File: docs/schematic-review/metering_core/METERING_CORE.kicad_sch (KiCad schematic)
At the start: 56 parts, among them U2 ATM90E26-YU, U4 ISO6721BD, U5 MAX3487E

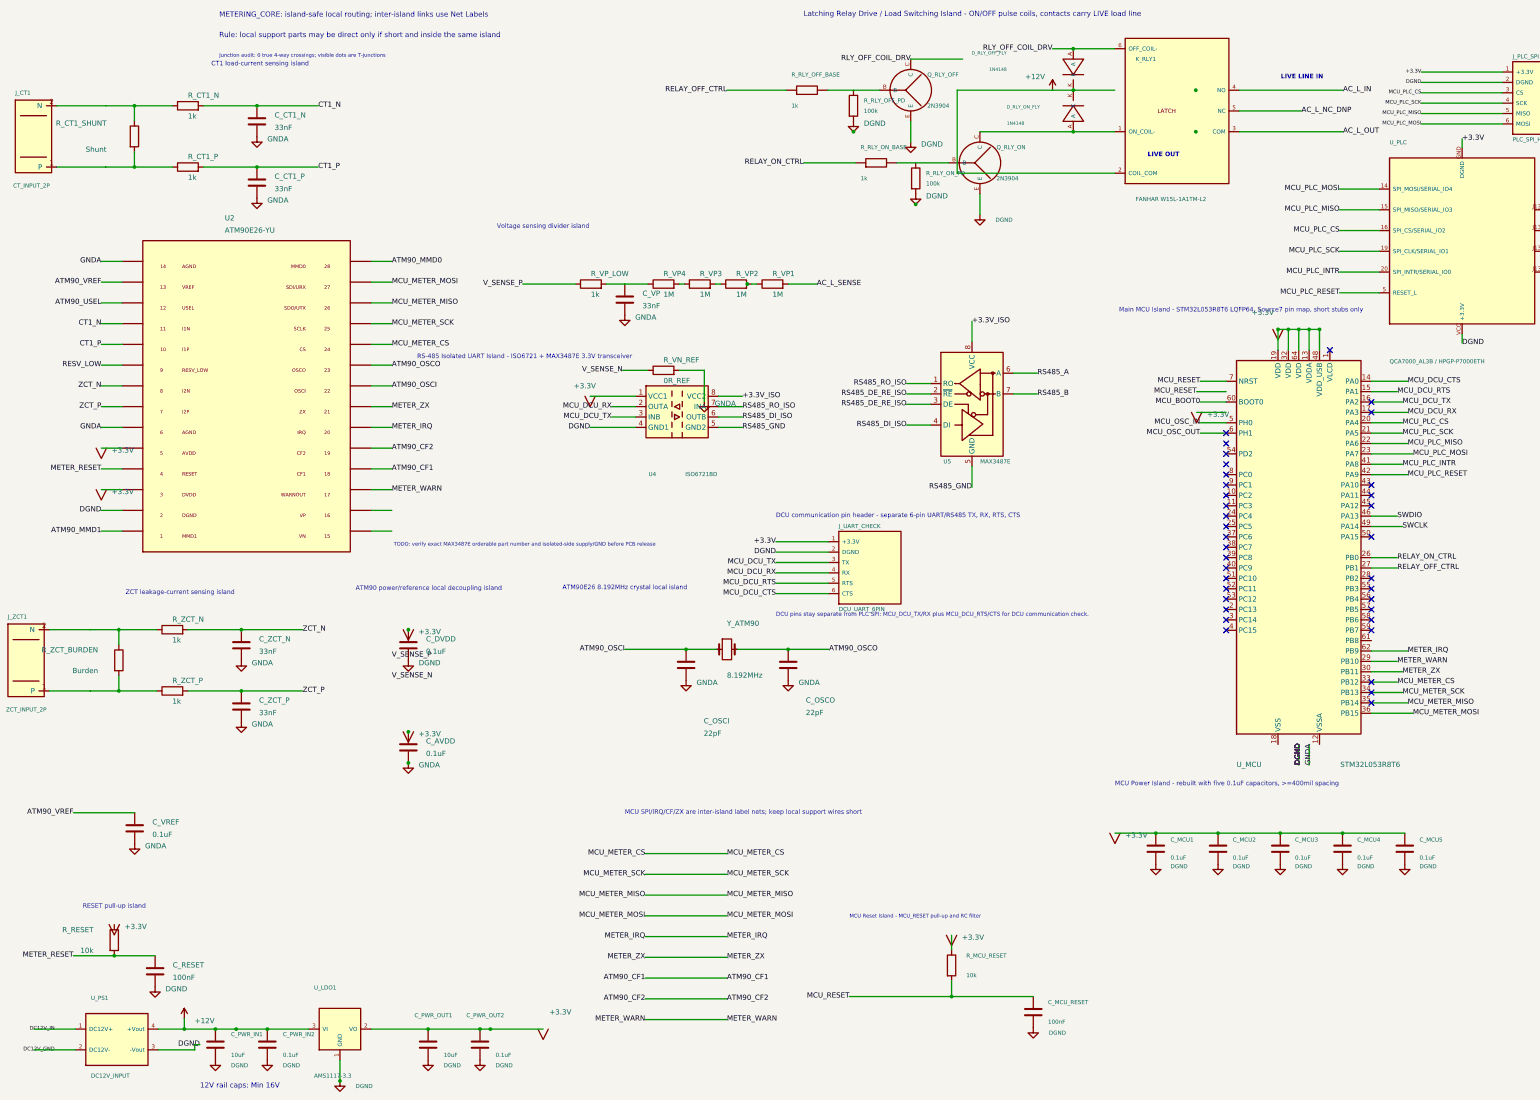
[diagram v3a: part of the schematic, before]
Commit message: Resolve metering schematic ERC review errors
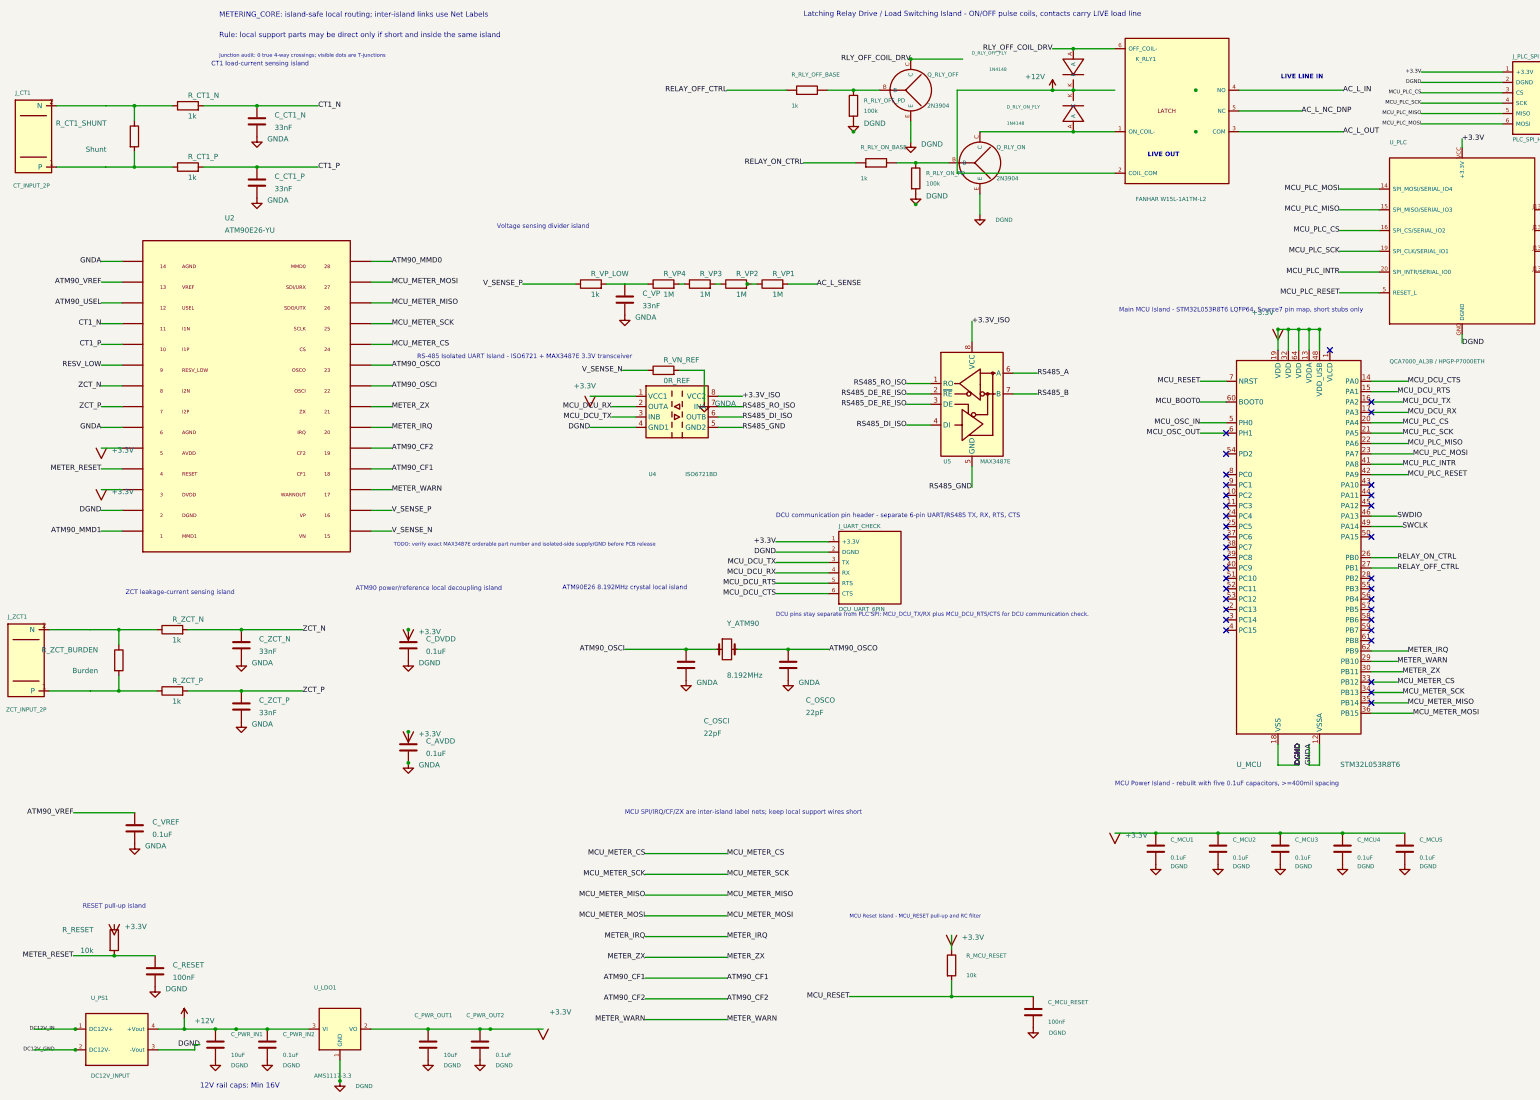
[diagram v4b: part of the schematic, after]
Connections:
- net +3.3V: now also U_PLC.VCC (+3.3V); no longer U_PLC.GND (DGND)
- net DGND: now also U_MCU.18 (VSS), U_PLC.GND (DGND); no longer U_PLC.VCC (+3.3V)
- net GNDA: now also U_MCU.12 (VSSA)
- net V_SENSE_N: now also U2.15 (VN)
- net V_SENSE_P: now also U2.16 (VP)
- net at R_RLY_ON_PD.1: now also Q_RLY_ON.B, R_RLY_ON_BASE.2
- net at R_RLY_OFF_PD.1: now also Q_RLY_OFF.B, R_RLY_OFF_BASE.2
- no-connect marks 36 -> 35
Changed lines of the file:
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@@
 	)
 	(no_connect
+		(at 347.78 172.86)
+	)
+	(no_connect
 		(at 312.22 134.76)
 	)
@@
 	)
 	(no_connect
-		(at 312.22 124.6)
-	)
-	(no_connect
 		(at 347.78 157.62)
 	)
@@
 	)
 	(no_connect
-		(at 312.22 129.68)
-	)
-	(no_connect
 		(at 347.78 134.76)
 	)
@@
 	(wire
 		(pts
+			(xy 324.92 198.26) (xy 324.92 203.34)
+		)
+		(stroke
+			(width 0)
+			(type solid)
+		)
+	)
+	(wire
+		(pts
+			(xy 324.92 203.34) (xy 330 203.34)
+		)
+		(stroke
+			(width 0)
+			(type solid)
+		)
+	)
+	(wire
+		(pts
 			(xy 102.87 95.25) (xy 107.95 95.25)
 		)
@@
 	(wire
 		(pts
+			(xy 335.08 198.26) (xy 335.08 203.34)
+		)
+		(stroke
+			(width 0)
+			(type solid)
+		)
+	)
+	(wire
+		(pts
+			(xy 332.54 203.34) (xy 335.08 203.34)
+		)
+		(stroke
+			(width 0)
+			(type solid)
+		)
+	)
+	(wire
+		(pts
 			(xy 187.17 85.56) (xy 188.44 85.56)
 		)
@@
 	(wire
 		(pts
-			(xy 312.22 111.9) (xy 305 111.9)
-		)
-		(stroke
-			(width 0)
-			(type solid)
-		)
-	)
-	(wire
-		(pts
 			(xy 58.03 185.18) (xy 86.12 185.18)
 		)
@@
 	(wire
 		(pts
-			(xy 312.22 116.98) (xy 305 116.98)
-		)
-		(stroke
-			(width 0)
-			(type solid)
-		)
-	)
-	(wire
-		(pts
 			(xy 330 101.74) (xy 330 96.66)
 		)
@@
 		)
 	)
-	(symbol
-		(lib_id "power:+3.3V")
-		(at 305 116.98 0)
-		(unit 1)
-		(body_style 1)
-		(exclude_from_sim no)
-		(in_bom yes)
-		(on_board yes)
-		(in_pos_files yes)
-		(dnp no)
-		(property "Reference" "#PWR_AUTO_33V_002"
-			(at 307.54 113.17 0)
-			(hide yes)
-			(show_name no)
-			(do_not_autoplace no)
-			(effects (font (size 1.27 1.27)))
-		)
-		(property "Value" "+3.3V"
-			(at 307.54 117.488 0)
-			(show_name no)
-			(do_not_autoplace no)
-			(effects (font (size 1.27 1.27)) (justify left))
-		)
-		(property "Footprint" ""
-			(at 305 116.98 0)
-			(show_name no)
-			(do_not_autoplace no)
-			(effects (font (size 1.27 1.27)))
-		)
-		(property "Datasheet" ""
-			(at 305 116.98 0)
-			(show_name no)
-			(do_not_autoplace no)
-			(effects (font (size 1.27 1.27)))
-		)
-		(property "Description" ""
-			(at 305 116.98 0)
-			(show_name no)
-			(do_not_autoplace no)
-			(effects (font (size 1.27 1.27)))
-		)
-		(pin "1")
-		(instances
-			(project "METERING_CORE"
-				(path "/e4236fbb-ccab-4d10-bcea-7fda722d6751"
-					(reference "#PWR_AUTO_33V_002")
-					(unit 1)
-				)
-			)
-		)
-	)
 	(label "SWDIO"
 		(at 354.13 142.38 0)
@@
 		)
 	)
-	(label "MCU_RESET"
-		(at 305 111.9 180)
-		(effects
-			(font
-				(size 1.27 1.27)
-			)
-			(justify right)
-		)
-	)
 	(label "SWCLK"
 		(at 355.4 144.92 0)
@@
 	)
 	(label "V_SENSE_N"
-		(at 107.95 181.61 0)
+		(at 107.95 146.05 0)
 		(effects
 			(font
@@
 	)
 	(label "V_SENSE_P"
-		(at 107.95 176.53 0)
+		(at 107.95 140.97 0)
 		(effects
 			(font
@@
 		(color 0 0 0 0)
 	)
+	(junction
+		(at 236.22 55.88)
+		(diameter 0)
+		(color 0 0 0 0)
+	)
 	(symbol
 		(lib_id "Device:R")
@@
 		(color 0 0 0 0)
 	)
+	(junction
+		(at 220.98 38.1)
+		(diameter 0)
+		(color 0 0 0 0)
+	)
+	(junction
+		(at 235 30.48)
+		(diameter 0)
+		(color 0 0 0 0)
+	)
+	(junction
+		(at 269.72 38.1)
+		(diameter 0)
+		(color 0 0 0 0)
+	)
+	(junction
+		(at 30.48 267.97)
+		(diameter 0)
+		(color 0 0 0 0)
+	)
+	(junction
+		(at 30.48 273.05)
+		(diameter 0)
+		(color 0 0 0 0)
+	)
 	(symbol
 		(lib_id "Device:R")
@@
 		(color 0 0 0 0)
 	)
+	(symbol
+		(lib_id "power:PWR_FLAG")
+		(at 193.8 113.03 0)
+		(unit 1)
+		(body_style 1)
+		(exclude_from_sim no)
+		(in_bom no)
+		(on_board no)
+		(in_pos_files no)
+		(dnp no)
+		(property "Reference" "#FLG_RS485_33V_ISO"
+			(at 193.8 110.49 0)
+			(hide yes)
+			(show_name no)
+			(do_not_autoplace no)
+			(effects (font (size 1 1)))
+		)
+		(property "Value" "PWR_FLAG"
+			(at 193.8 115.57 0)
+			(hide yes)
+			(show_name no)
+			(do_not_autoplace no)
+			(effects (font (size 1 1)))
+		)
+		(property "Footprint" "" (at 193.8 113.03 0) (hide yes) (show_name no) (do_not_autoplace no) (effects (font (size 1 1))))
+		(property "Datasheet" "" (at 193.8 113.03 0) (hide yes) (show_name no) (do_not_autoplace no) (effects (font (size 1 1))))
+		(property "Description" "" (at 193.8 113.03 0) (hide yes) (show_name no) (do_not_autoplace no) (effects (font (size 1 1))))
+		(pin "1")
+		(instances (project "METERING_CORE" (path "/e4236fbb-ccab-4d10-bcea-7fda722d6751" (reference "#FLG_RS485_33V_ISO") (unit 1))))
+	)
+	(symbol
+		(lib_id "power:PWR_FLAG")
+		(at 193.8 120.65 0)
+		(unit 1)
+		(body_style 1)
+		(exclude_from_sim no)
+		(in_bom no)
+		(on_board no)
+		(in_pos_files no)
+		(dnp no)
+		(property "Reference" "#FLG_RS485_GND"
+			(at 193.8 118.11 0)
+			(hide yes)
+			(show_name no)
+			(do_not_autoplace no)
+			(effects (font (size 1 1)))
+		)
+		(property "Value" "PWR_FLAG"
+			(at 193.8 123.19 0)
+			(hide yes)
+			(show_name no)
+			(do_not_autoplace no)
+			(effects (font (size 1 1)))
+		)
+		(property "Footprint" "" (at 193.8 120.65 0) (hide yes) (show_name no) (do_not_autoplace no) (effects (font (size 1 1))))
+		(property "Datasheet" "" (at 193.8 120.65 0) (hide yes) (show_name no) (do_not_autoplace no) (effects (font (size 1 1))))
+		(property "Description" "" (at 193.8 120.65 0) (hide yes) (show_name no) (do_not_autoplace no) (effects (font (size 1 1))))
+		(pin "1")
+		(instances (project "METERING_CORE" (path "/e4236fbb-ccab-4d10-bcea-7fda722d6751" (reference "#FLG_RS485_GND") (unit 1))))
+	)
 	(sheet_instances
